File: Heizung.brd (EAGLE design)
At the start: 100 x 80 mm, 34 parts, among them IC1 MEGA8-PTQFP, Q2 2N7002, Q3 2N7002

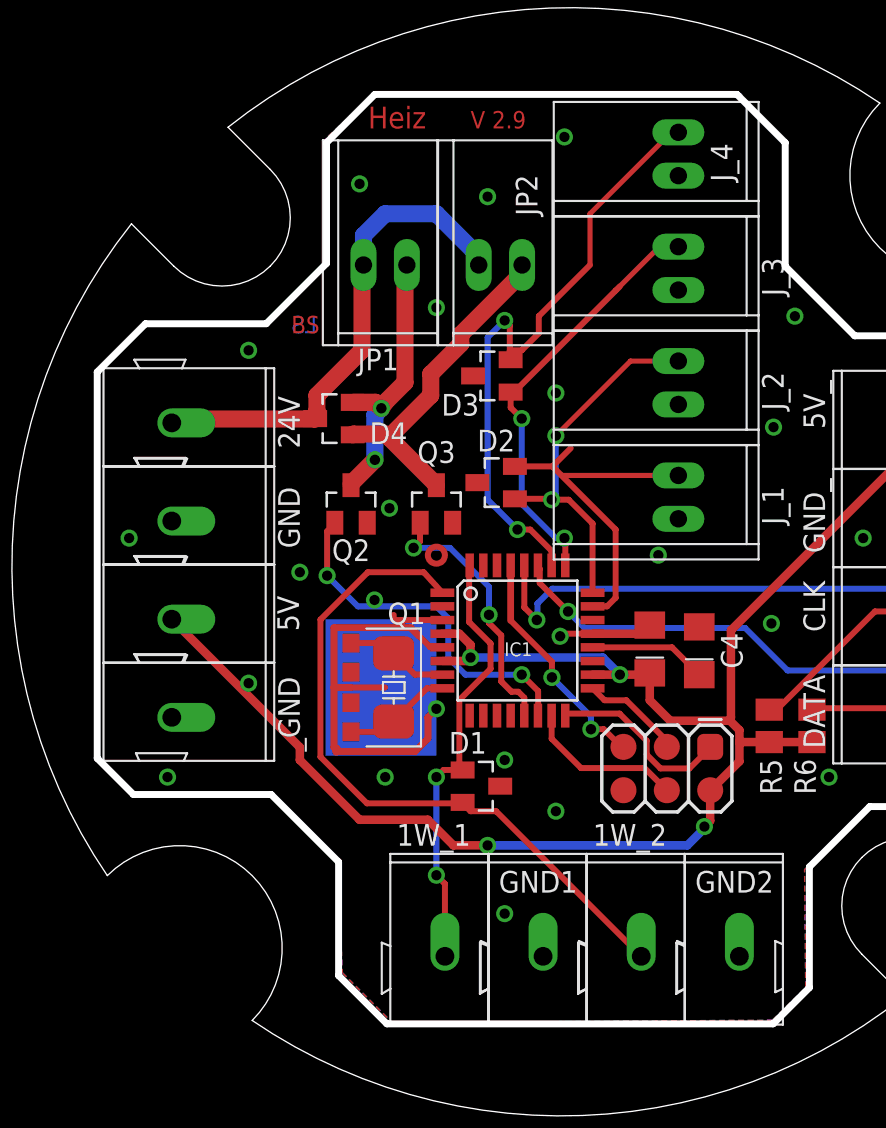
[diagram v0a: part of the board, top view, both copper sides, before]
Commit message: v3.0: use separate ground for switched power (24V)
otherwise long cabling will raise ground too much
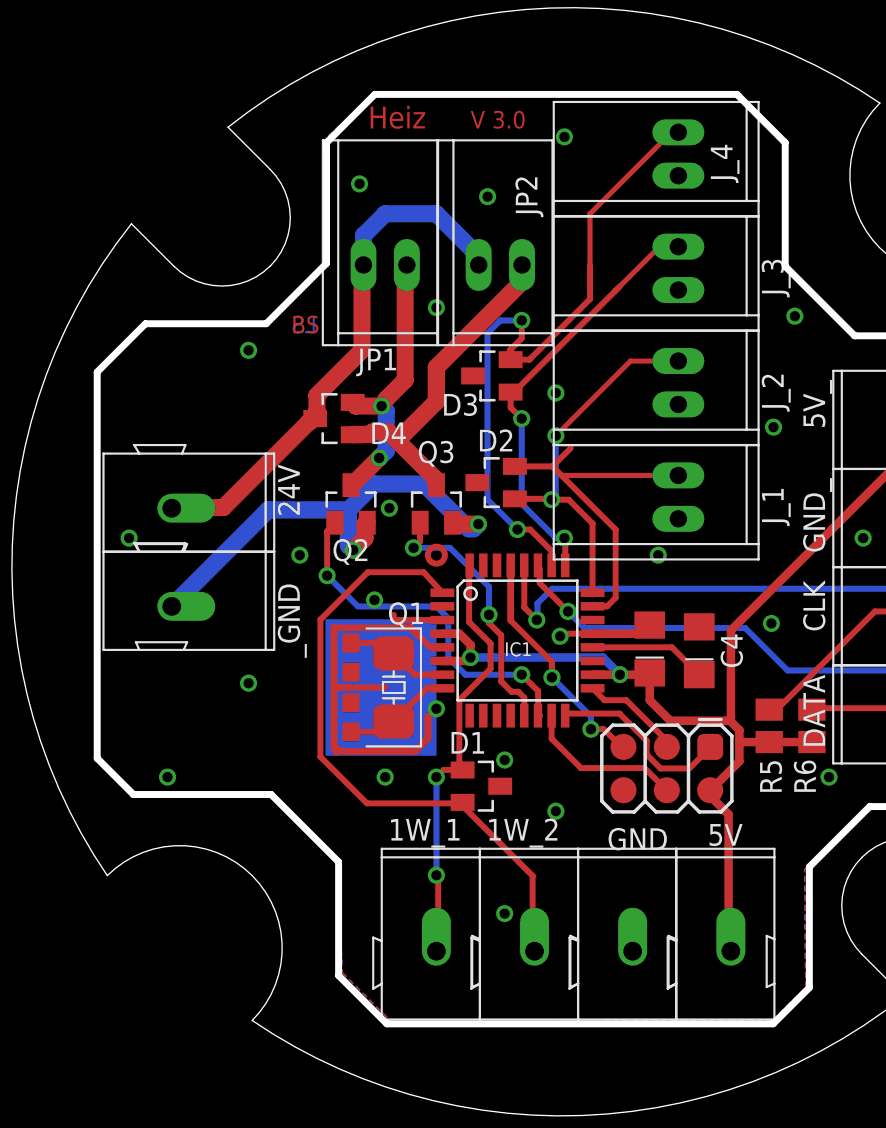
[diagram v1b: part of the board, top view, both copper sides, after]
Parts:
- removed GND1, GND2: WAGO_243, common:WAGO_243
- moved 5V 38.1 mm to (44.2, 23.8), turned to 90 degrees
- moved B_GND 36.9 mm to (38.5, 23.8), turned to 90 degrees
- moved _GND 6.50 mm to (11.5, 44.0)
- moved 1W_2 6.26 mm to (32.8, 23.8)
- moved 24V 5.00 mm to (11.5, 49.8)
- moved 1W_1 0.58 mm to (27.0, 23.8)
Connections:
- new net GND24: Q2.2, Q3.2, _GND.P$1
- net GND: no longer GND1.P$1, GND2.P$1, Q2.2, Q3.2, _GND.P$1
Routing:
- net 5V: track 99.9 -> 69.9 mm, vias 4 -> 2
- net GND24: track 0.00 -> 28.1 mm, vias 0 -> 2
- net N$8: track 40.7 -> 37.0 mm
- net B4: track 36.7 -> 38.9 mm
- net N$1: track 29.2 -> 31.2 mm
- net N$33: track 19.5 -> 19.9 mm, vias 0 -> 1
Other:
- board text added: "V 3.0"
- board text removed: "V 2.9"

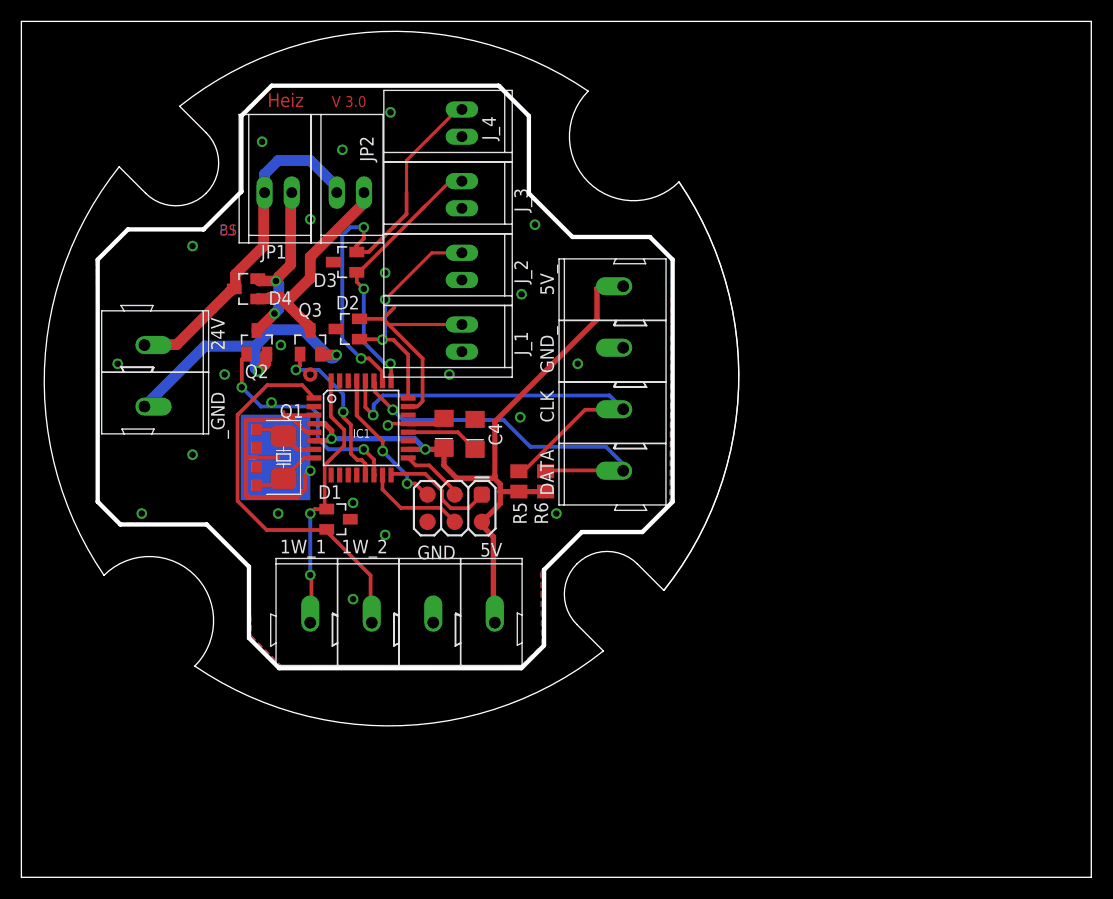
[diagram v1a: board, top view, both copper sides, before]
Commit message: V 3.2: secondary I²C yes, secondary 1wire no
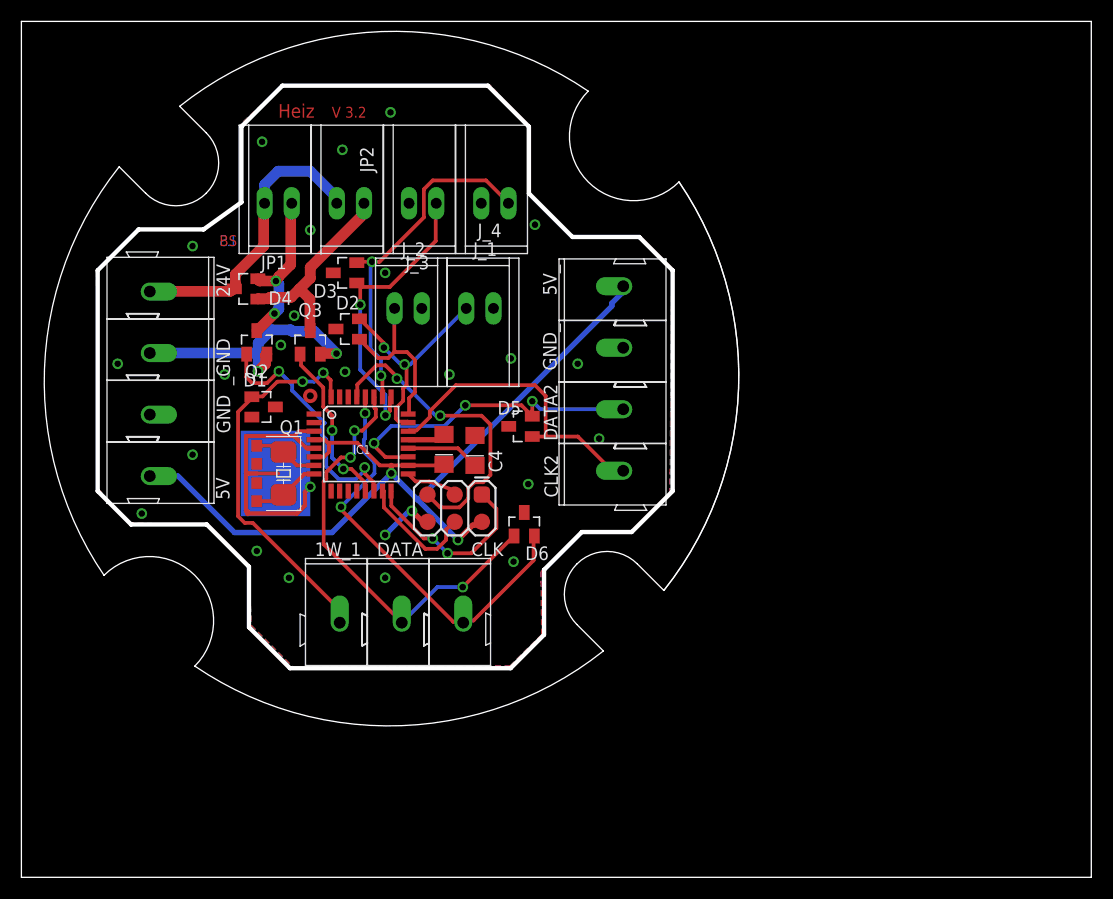
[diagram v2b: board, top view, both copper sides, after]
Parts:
- removed 1W_2: WAGO_243, common:WAGO_243
- removed R5, R6: (no value), common:M0805
- added CLK2, DATA2: WAGO_243, common:WAGO_243
- added D5, D6: ESD_DIODES, common:SOT23
- moved 5V 35.0 mm to (12.0, 37.5), turned to 0 degrees
- moved B_GND 32.9 mm to (12.0, 43.2), turned to 0 degrees
- moved DATA 25.1 mm to (35.5, 23.8), turned to 90 degrees
- moved CLK 24.9 mm to (41.3, 23.8), turned to 90 degrees
- moved D1 12.6 mm to (22.6, 44.0)
- moved J_4 8.11 mm to (44.2, 63.0), turned to 0 degrees
- moved J_2 6.38 mm to (36.1, 53.2), turned to 180 degrees
- moved 24V 5.02 mm to (12.0, 54.8)
- moved _GND 5.02 mm to (12.0, 49.0)
- moved J_3 3.76 mm to (37.5, 63.0), turned to 0 degrees
- moved J_1 3.24 mm to (42.9, 53.2), turned to 180 degrees
- moved 1W_1 2.75 mm to (29.8, 23.8)
- moved C1 1.50 mm to (39.5, 40.0)
- moved C2 1.50 mm to (22.0, 39.5)
- moved C3 1.50 mm to (22.0, 36.0)
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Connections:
- removed net 5V: 5V.P$1, 5V_.P$1, C1.+, IC1.18, IC1.4, IC1.6, R5.2, R6.2, U$3.P$2
- removed net N$8: 1W_2.P$1, D1.2, IC1.1
- new net +5V: 5V.P$1, 5V_.P$1, C1.+, IC1.18, IC1.4, IC1.6, U$3.P$2
- new net B5: D5.2, DATA2.P$1, IC1.19
- new net B6: CLK2.P$1, D5.1, IC1.22
- net GND: now also D5.3, D6.3
- net N$10: now also D6.1; no longer R6.1
- net N$18: now also D6.2; no longer R5.1
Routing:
- net +5V: track 0.00 -> 84.1 mm, vias 0 -> 2
- net 5V: track 69.9 -> 0.00 mm, vias 2 -> 0
- net N$8: track 37.0 -> 0.00 mm
- net B5: track 0.00 -> 31.1 mm, vias 0 -> 3
- net B6: track 0.00 -> 29.0 mm
- net N$37: track 14.2 -> 29.7 mm
- net N$5: track 25.5 -> 36.2 mm
- net N$35: track 10.9 -> 17.7 mm, vias 0 -> 2
- net B2: track 22.0 -> 15.9 mm, vias 2 -> 0
- net N$10: track 35.1 -> 41.0 mm, vias 1 -> 3
- net B4: track 38.9 -> 33.0 mm
- net N$1: track 31.2 -> 27.7 mm
- net GND24: track 28.1 -> 25.2 mm
- net B3: track 25.5 -> 28.3 mm
- net N$3: track 21.4 -> 24.1 mm
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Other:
- outline, holes or cut-outs redrawn
- board text added: "V 3.2"
- board text removed: "V 3.0"
